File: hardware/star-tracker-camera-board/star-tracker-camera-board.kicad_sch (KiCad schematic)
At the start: 41 parts, among them J1 3-1734742-6, U1 AR0134CSSM00SPCA0, U2 TPS70618DRVR, U3 TPS71928-28DRVT, U4 TPS71928-28DRVT, X1 KC2520B27.0000C10E00

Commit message: More EAGLE import clean up
Fixed BOM, still needs 0402 passives. Fixed ERCs, and a bunch of DRCs. U1 still needs footprint cleanup.
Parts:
- C10, C14, C6: DIS (none) -> DigiKey; DPN (none) -> 490-GRT188R71E105KE13DCT-ND; MFR (none) -> Murata Electronics; MPN (none) -> GRT188R71E105KE13D
- C11, C15, C18, C19, C7: DIS (none) -> DigiKey; DPN (none) -> 490-GRT188C71E225KE13DCT-ND; MFR (none) -> Murata Electronics; MPN (none) -> GRT188C71E225KE13D
- J1: DIS (none) -> DigiKey; DPN (none) -> A100241CT-ND; MFR (none) -> TE; MPN (none) -> 3-1734742-6
- TP10, TP6, TP7, TP8, TP9: now left out of the parts list
- U1: DIS (none) -> DigiKey; DPN (none) -> 5556-AR0134CSSM00SPCA0-DPBR-ND; MFR (none) -> OnSemi; MPN (none) -> AR0134CSSM00SPCA0
- U2: DIS (none) -> DigiKey; DPN (none) -> 296-48768-1-ND; MFR (none) -> TI; MPN (none) -> TPS70618DRVR
- U3, U4: DIS (none) -> DigiKey; DPN (none) -> 296-TPS71928-28DRVTCT-ND; MFR (none) -> TI; MPN (none) -> TPS71928-28DRVT
- X1: DIS (none) -> DigiKey; DPN (none) -> OBSOLETE; MFR (none) -> Kyocera; MPN (none) -> KC2520B27.0000C10E00
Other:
- company: (none) -> Portland State Aerospace Society
- title: (none) -> Oresat Star Tracker Camera Board
- moved on the sheet: C1, C10, C11, C12, C13, C14, C15, C16, C17, C18, C19, C2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

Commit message: Updated BOM for daughterboard
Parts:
- C1: DIS (none) -> Digikey; DPN (none) -> 399-19365-1-ND; MFR (none) -> KEMET; MPN (none) -> C0402C103J5RACAUTO
- C12, C16, C2, C4, C8: DIS (none) -> Digikey; DPN (none) -> 399-C2220X106J5RACAUTOTR-ND; MFR (none) -> KEMET; MPN (none) -> C2220X106J5RACAUTO
- C13, C17, C3, C5, C9: DIS (none) -> Digikey; DPN (none) -> 399-17548-1-ND; MFR (none) -> KEMET; MPN (none) -> C0402C104J4RACAUTO
- R10, R11, R12, R9: DIS (none) -> Digikey; DPN (none) -> 738-RMCA0402FT10K0-HPCT-ND; MFR (none) -> Stackpole Electronics; MPN (none) -> RMCA0402FT10K0-HP
- R2: DIS (none) -> Digikey; DPN (none) -> 738-RMCA0402FT100R-HPCT-ND; MFR (none) -> Stackpole Electronics Inc; MPN (none) -> RMCA0402FT100R-HP
- R3, R6: DIS (none) -> Digikey
- R4, R5: DIS (none) -> Digikey; DPN (none) -> 738-RNCP0402FTD10K0CT-ND; MFR (none) -> Stackpole Electronics; MPN (none) -> RNCP0402FTD10K0
- R7, R8: DIS (none) -> Digikey; DPN (none) -> 738-RMCA0402FT4K70-HPCT-ND; MFR (none) -> Stackpole Electronics; MPN (none) -> RMCA0402FT4K70-HP

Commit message: Revised BOM
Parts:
- C12, C16, C2, C4, C8: DPN 399-C2220X106J5RACAUTOTR-ND -> 490-12286-1-ND; MFR KEMET -> Murata Electronics; MPN C2220X106J5RACAUTO -> GRT188C81C106ME13D
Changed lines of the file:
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@@
 			)
 		)
-		(property "DPN" "399-C2220X106J5RACAUTOTR-ND"
+		(property "DPN" "490-12286-1-ND"
 			(at 334.01 43.18 0)
 			(effects
@@
 			)
 		)
-		(property "MFR" "KEMET"
+		(property "MFR" "Murata Electronics"
 			(at 334.01 43.18 0)
 			(effects
@@
 			)
 		)
-		(property "MPN" "C2220X106J5RACAUTO"
+		(property "MPN" "GRT188C81C106ME13D"
 			(at 334.01 43.18 0)
 			(effects
@@
 			)
 		)
-		(property "DPN" "399-C2220X106J5RACAUTOTR-ND"
+		(property "DPN" "490-12286-1-ND"
 			(at 323.85 43.18 0)
 			(effects
@@
 			)
 		)
-		(property "MFR" "KEMET"
+		(property "MFR" "Murata Electronics"
 			(at 323.85 43.18 0)
 			(effects
@@
 			)
 		)
-		(property "MPN" "C2220X106J5RACAUTO"
+		(property "MPN" "GRT188C81C106ME13D"
 			(at 323.85 43.18 0)
 			(effects
@@
 			)
 		)
-		(property "DPN" "399-C2220X106J5RACAUTOTR-ND"
+		(property "DPN" "490-12286-1-ND"
 			(at 303.53 43.18 0)
 			(effects
@@
 			)
 		)
-		(property "MFR" "KEMET"
+		(property "MFR" "Murata Electronics"
 			(at 303.53 43.18 0)
 			(effects
@@
 			)
 		)
-		(property "MPN" "C2220X106J5RACAUTO"
+		(property "MPN" "GRT188C81C106ME13D"
 			(at 303.53 43.18 0)
 			(effects
@@
 			)
 		)
-		(property "DPN" "399-C2220X106J5RACAUTOTR-ND"
+		(property "DPN" "490-12286-1-ND"
 			(at 293.37 43.18 0)
 			(effects
@@
 			)
 		)
-		(property "MFR" "KEMET"
+		(property "MFR" "Murata Electronics"
 			(at 293.37 43.18 0)
 			(effects
@@
 			)
 		)
-		(property "MPN" "C2220X106J5RACAUTO"
+		(property "MPN" "GRT188C81C106ME13D"
 			(at 293.37 43.18 0)
 			(effects
@@
 			)
 		)
-		(property "DPN" "399-C2220X106J5RACAUTOTR-ND"
+		(property "DPN" "490-12286-1-ND"
 			(at 313.69 43.18 0)
 			(effects
@@
 			)
 		)
-		(property "MFR" "KEMET"
+		(property "MFR" "Murata Electronics"
 			(at 313.69 43.18 0)
 			(effects
@@
 			)
 		)
-		(property "MPN" "C2220X106J5RACAUTO"
+		(property "MPN" "GRT188C81C106ME13D"
 			(at 313.69 43.18 0)
 			(effects

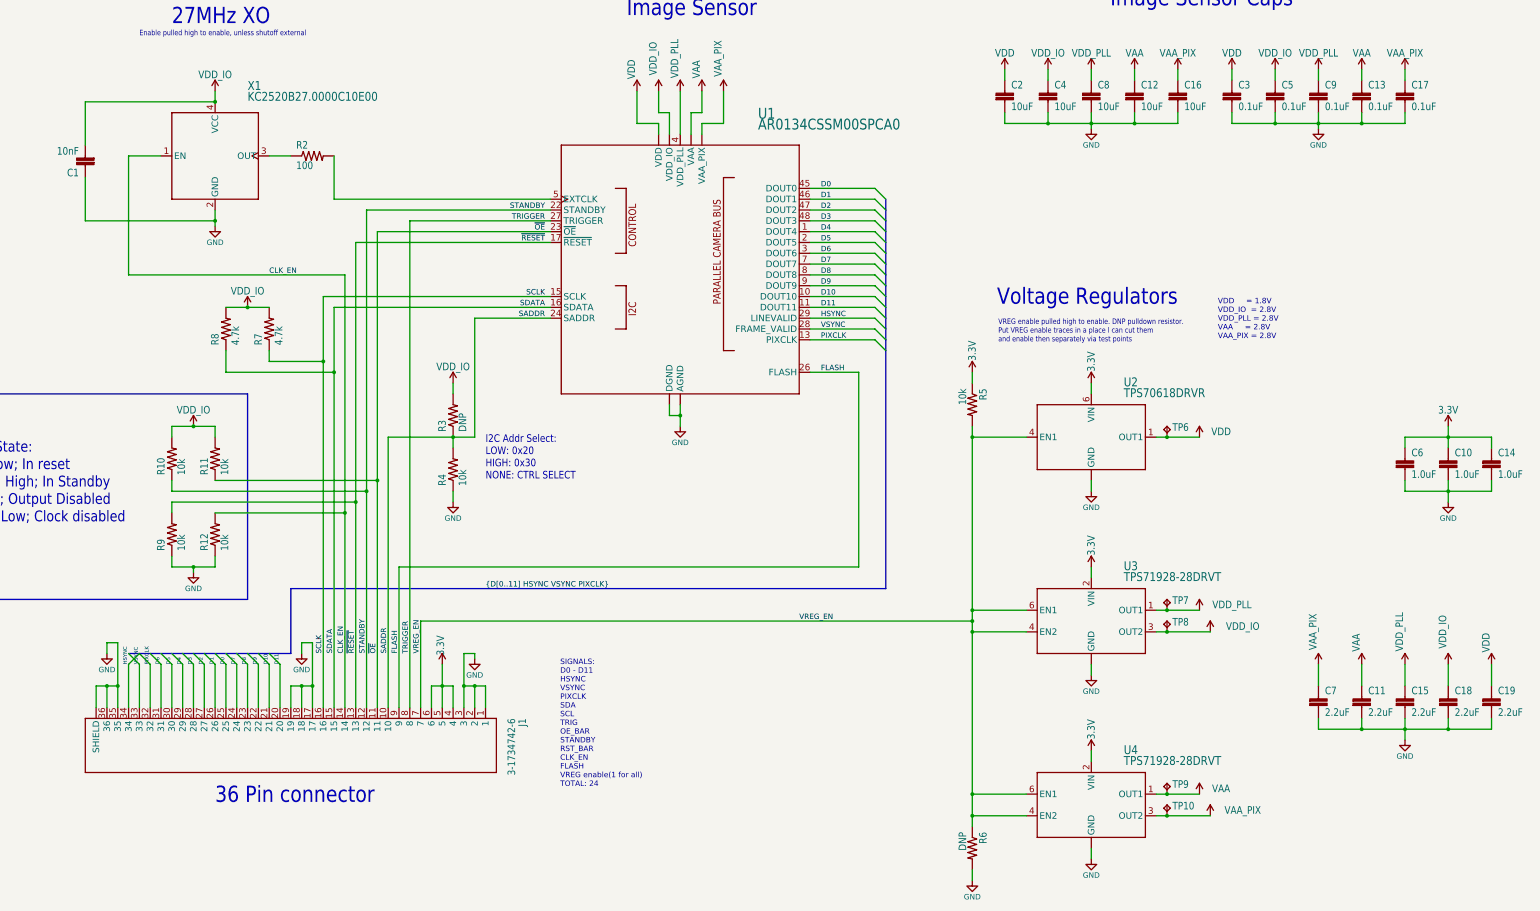
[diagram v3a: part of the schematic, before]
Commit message: Updated schematic
Updated schematic symbols footprints and replaced EOL osc. Rearranged component designators.
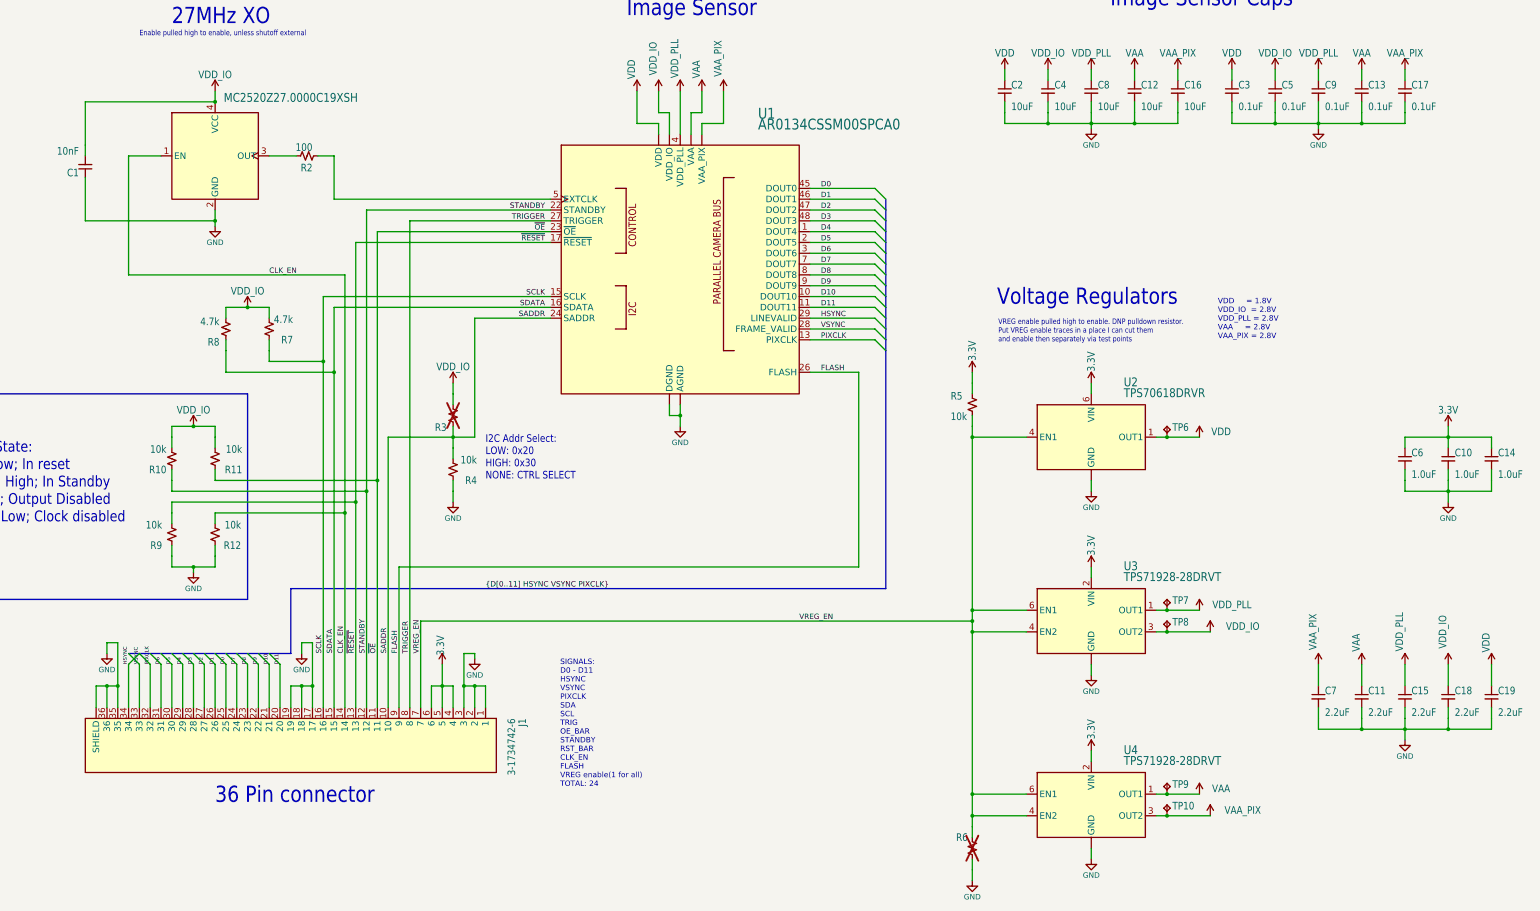
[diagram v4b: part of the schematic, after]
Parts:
- removed X1: KC2520B27.0000C10E00, star-tracker-camera-board:OSC_KYOCERA_KC2520B, symbol star-tracker-camera-board-eagle-import:KC2520B27.0000C10E00
- added X1: MC2520Z27.0000C19XSH, star-tracker-camera-board:OSC_KYOCERA_KC2520B, symbol star-tracker-camera-board-eagle-import:MC2520Z27.0000C19XSH
- C1: footprint star-tracker-camera-board:.0402-A-NOSILK -> oresat-passives:0402-B-NOSILK; symbol star-tracker-camera-board-eagle-import:C-EU0402-A-NOSILK -> Device:C_Small
- C10, C11, C12, C14, C15, C16, C18, C19, C2, C4, C6, C7, C8: footprint star-tracker-camera-board:.0603-C-NOSILK -> oresat-passives:c_0603-SMALL; symbol star-tracker-camera-board-eagle-import:C-EU0603-C-NOSILK -> Device:C_Small
- C13, C17, C3, C5, C9: footprint star-tracker-camera-board:.0402-B-NOSILK -> oresat-passives:0402-B-NOSILK; symbol star-tracker-camera-board-eagle-import:C-EU0402-B-NOSILK -> Device:C_Small
- R10, R11, R12, R2, R9: footprint star-tracker-camera-board:.0402-B -> oresat-passives:0402-B-NOSILK; symbol star-tracker-camera-board-eagle-import:R-US_0402-B -> Device:R_Small_US
- R3, R6: symbol star-tracker-camera-board-eagle-import:R-US_0402-B-NOSILK -> Device:R_Small_US; now not fitted
- R4, R5, R7, R8: footprint star-tracker-camera-board:.0402-B-NOSILK -> oresat-passives:0402-B-NOSILK; symbol star-tracker-camera-board-eagle-import:R-US_0402-B-NOSILK -> Device:R_Small_US
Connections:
- net CLK_EN: now also X1.1 (EN)
- net GND: now also X1.2 (GND)
- net VDD_IO: now also X1.4 (VCC)
- net at R2.1: now also X1.3 (OUT)

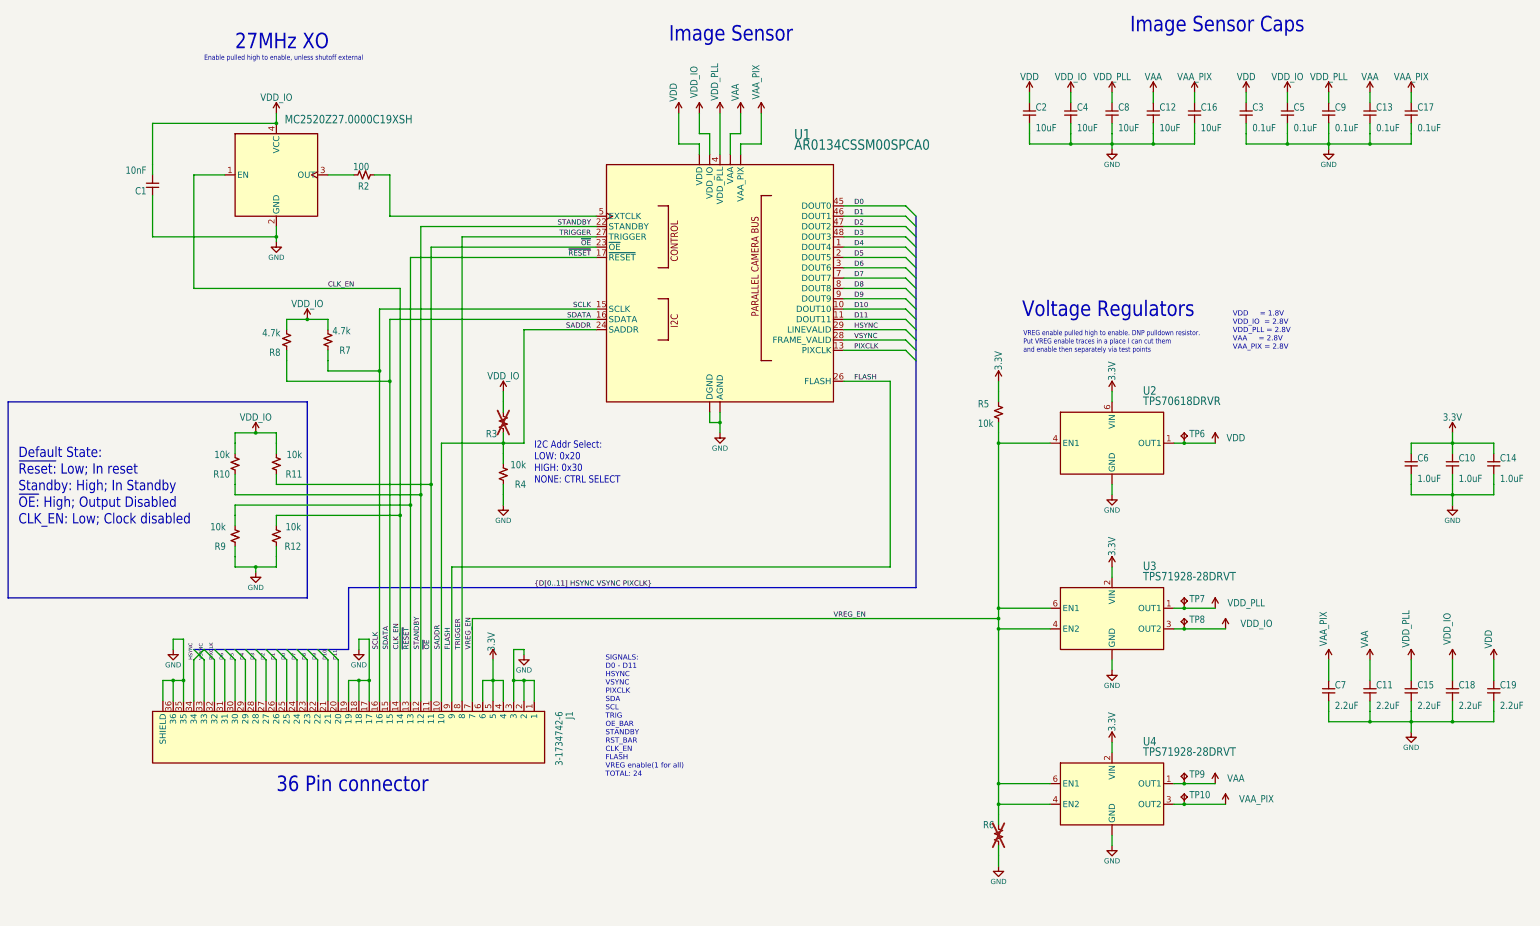
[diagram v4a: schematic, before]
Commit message: Fixed library links and updated footprints to the latest.
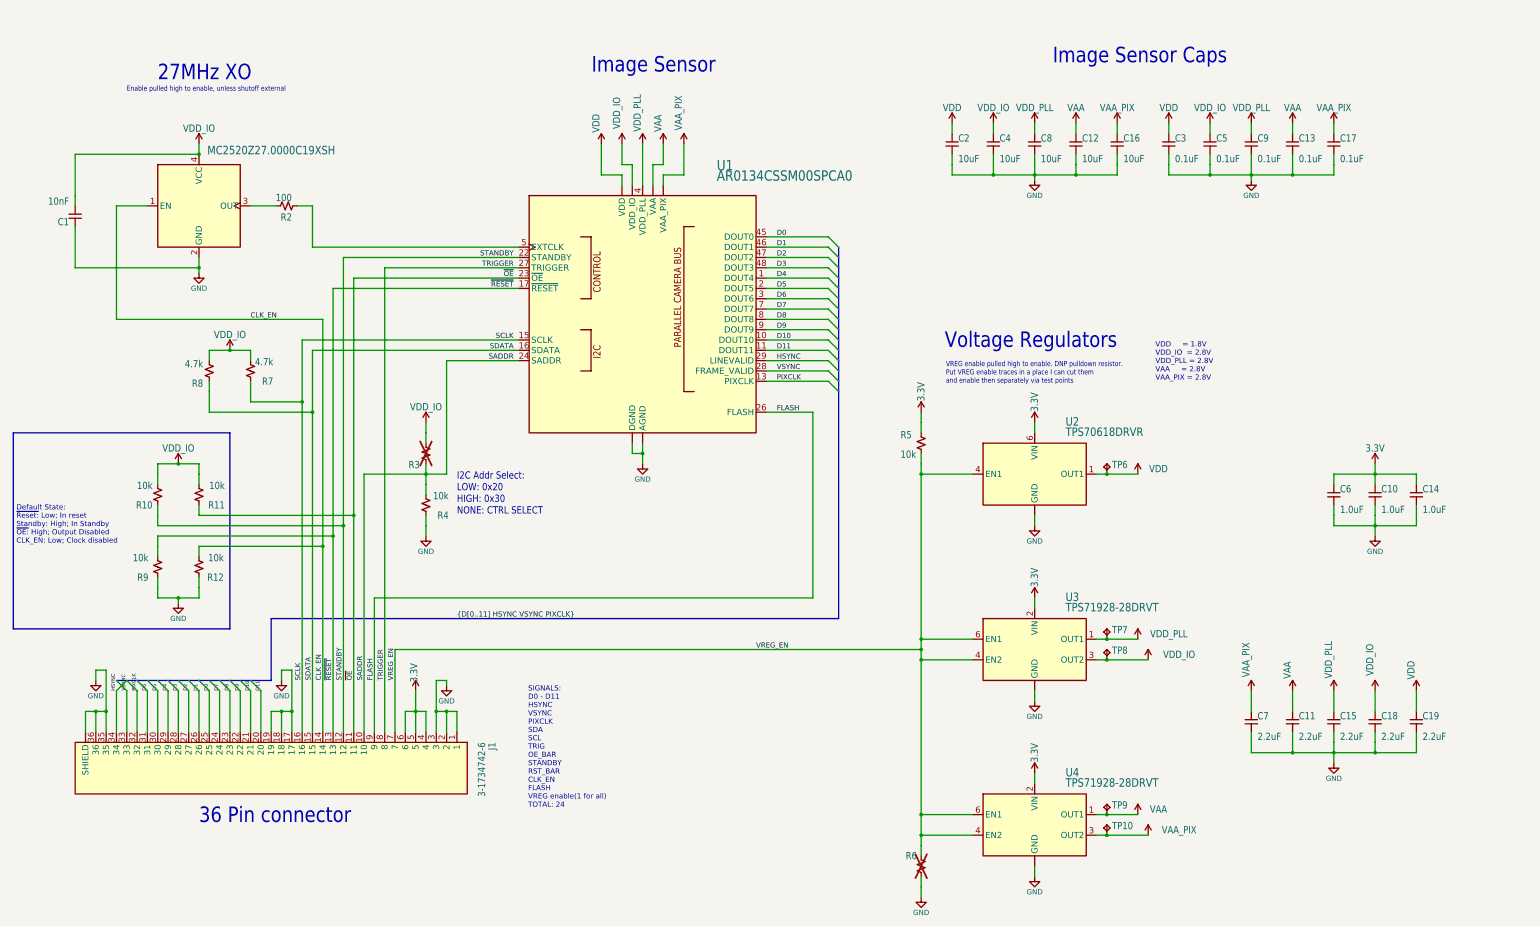
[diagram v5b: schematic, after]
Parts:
- C10, C14, C6: footprint oresat-passives:c_0603-SMALL -> oresat-passives:0402-B-NOSILK
- C11, C12, C15, C16, C18, C19, C2, C4, C7, C8: footprint oresat-passives:c_0603-SMALL -> oresat-passives:0603-C-NOSILK
- R10, R11, R12, R9: DPN 738-RMCA0402FT10K0-HPCT-ND -> RMCF0402FT10K0CT-ND; MPN RMCA0402FT10K0-HP -> RMCF0402FT10K0
- R2: DPN 738-RMCA0402FT100R-HPCT-ND -> RMCF0402FT100RCT-ND; MPN RMCA0402FT100R-HP -> RMCF0402FT100R
- R4, R5: DPN 738-RNCP0402FTD10K0CT-ND -> RMCF0402FT10K0CT-ND; MPN RNCP0402FTD10K0 -> RMCF0402FT10K0
- R7, R8: DPN 738-RMCA0402FT4K70-HPCT-ND -> RMCF0402FT4K70CT-ND; MPN RMCA0402FT4K70-HP -> RMCF0402FT4K70
- X1: DIS (none) -> DigiKey; DPN (none) -> 478-MC2520Z27.0000C19XSHCT-ND; MFR (none) -> KYOCERA AVX; MPN (none) -> MC2520Z27.0000C19XSH
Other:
- moved on the sheet: C1, C10, C11, C12, C13, C14, C15, C16, C17, C18, C19, C2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

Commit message: No significant update, just aesthetics and upgrade to KiCad 10.0.3
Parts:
- C10, C14, C6: DPN 490-GRT188R71E105KE13DCT-ND -> 490-18215-1-ND; MPN GRT188R71E105KE13D -> GRT155C81E105KE13D
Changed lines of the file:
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@@
 			)
 		)
-		(property "Datasheet" "https://search.murata.co.jp/Ceramy/image/img/A01X/G101/ENG/GRT188R71E105KE13-01.pdf"
+		(property "Datasheet" "https://search.murata.co.jp/Ceramy/image/img/A01X/G101/ENG/GRT155C81E105KE13-01.pdf"
 			(at 378.46 137.16 0)
 			(hide yes)
@@
 			)
 		)
-		(property "Description" "1 µF ±10% 25V Ceramic Capacitor X7R 0603 (1608 Metric)"
+		(property "Description" "1 µF ±10% 25V Ceramic Capacitor X6S 0402 (1005 Metric)"
 			(at 378.46 137.16 0)
 			(hide yes)
@@
 			)
 		)
-		(property "DPN" "490-GRT188R71E105KE13DCT-ND"
+		(property "DPN" "490-18215-1-ND"
 			(at 378.46 137.16 0)
 			(hide yes)
@@
 			)
 		)
-		(property "MPN" "GRT188R71E105KE13D"
+		(property "MPN" "GRT155C81E105KE13D"
 			(at 378.46 137.16 0)
 			(hide yes)
@@
 			)
 		)
-		(property "Datasheet" "https://search.murata.co.jp/Ceramy/image/img/A01X/G101/ENG/GRT188R71E105KE13-01.pdf"
+		(property "Datasheet" "https://search.murata.co.jp/Ceramy/image/img/A01X/G101/ENG/GRT155C81E105KE13-01.pdf"
 			(at 368.3 137.16 0)
 			(hide yes)
@@
 			)
 		)
-		(property "Description" "1 µF ±10% 25V Ceramic Capacitor X7R 0603 (1608 Metric)"
+		(property "Description" "1 µF ±10% 25V Ceramic Capacitor X6S 0402 (1005 Metric)"
 			(at 368.3 137.16 0)
 			(hide yes)
@@
 			)
 		)
-		(property "DPN" "490-GRT188R71E105KE13DCT-ND"
+		(property "DPN" "490-18215-1-ND"
 			(at 368.3 137.16 0)
 			(hide yes)
@@
 			)
 		)
-		(property "MPN" "GRT188R71E105KE13D"
+		(property "MPN" "GRT155C81E105KE13D"
 			(at 368.3 137.16 0)
 			(hide yes)
@@
 			)
 		)
-		(property "Datasheet" "https://search.murata.co.jp/Ceramy/image/img/A01X/G101/ENG/GRT188R71E105KE13-01.pdf"
+		(property "Datasheet" "https://search.murata.co.jp/Ceramy/image/img/A01X/G101/ENG/GRT155C81E105KE13-01.pdf"
 			(at 388.62 137.16 0)
 			(hide yes)
@@
 			)
 		)
-		(property "Description" "1 µF ±10% 25V Ceramic Capacitor X7R 0603 (1608 Metric)"
+		(property "Description" "1 µF ±10% 25V Ceramic Capacitor X6S 0402 (1005 Metric)"
 			(at 388.62 137.16 0)
 			(hide yes)
@@
 			)
 		)
-		(property "DPN" "490-GRT188R71E105KE13DCT-ND"
+		(property "DPN" "490-18215-1-ND"
 			(at 388.62 137.16 0)
 			(hide yes)
@@
 			)
 		)
-		(property "MPN" "GRT188R71E105KE13D"
+		(property "MPN" "GRT155C81E105KE13D"
 			(at 388.62 137.16 0)
 			(hide yes)
